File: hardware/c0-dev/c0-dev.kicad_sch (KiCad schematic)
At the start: 0 parts

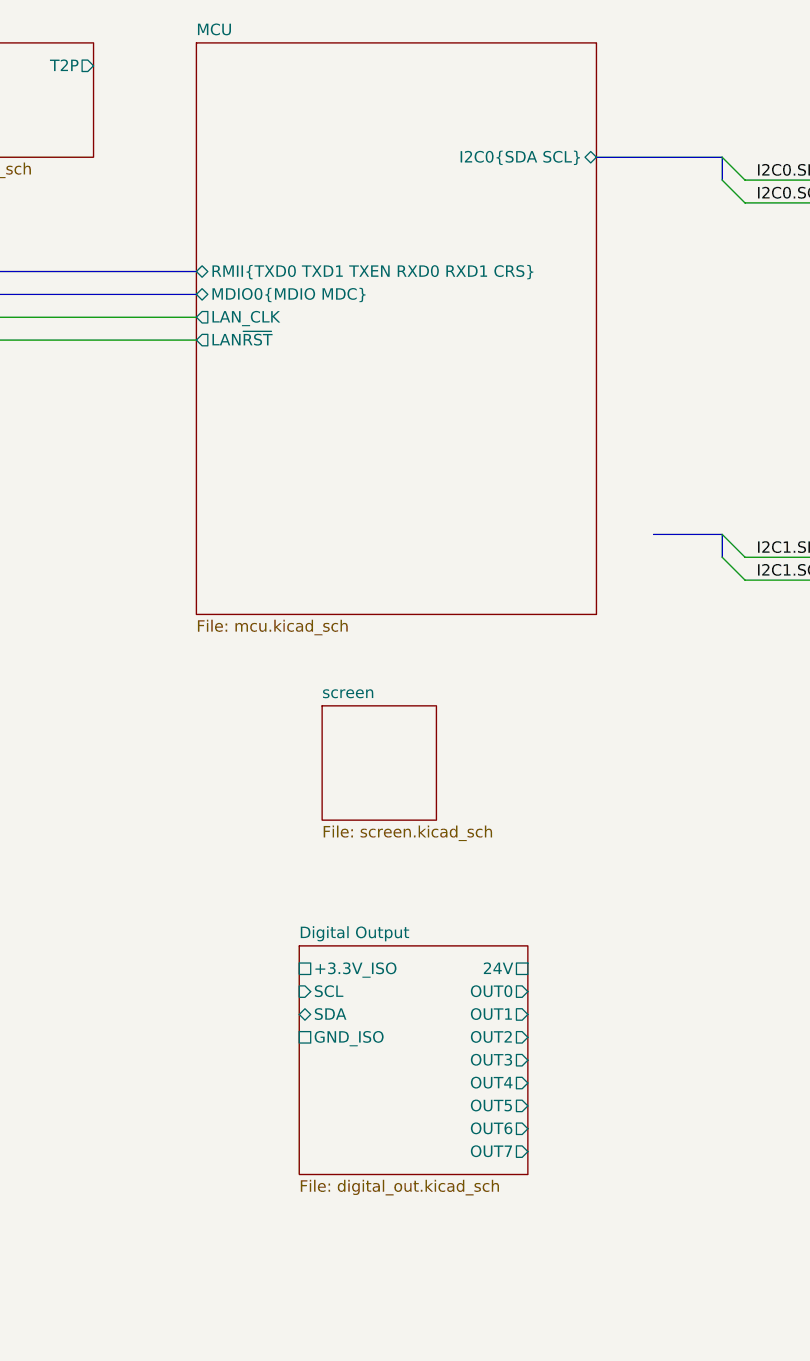
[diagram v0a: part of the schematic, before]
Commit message: introduced MCU isolation netclass
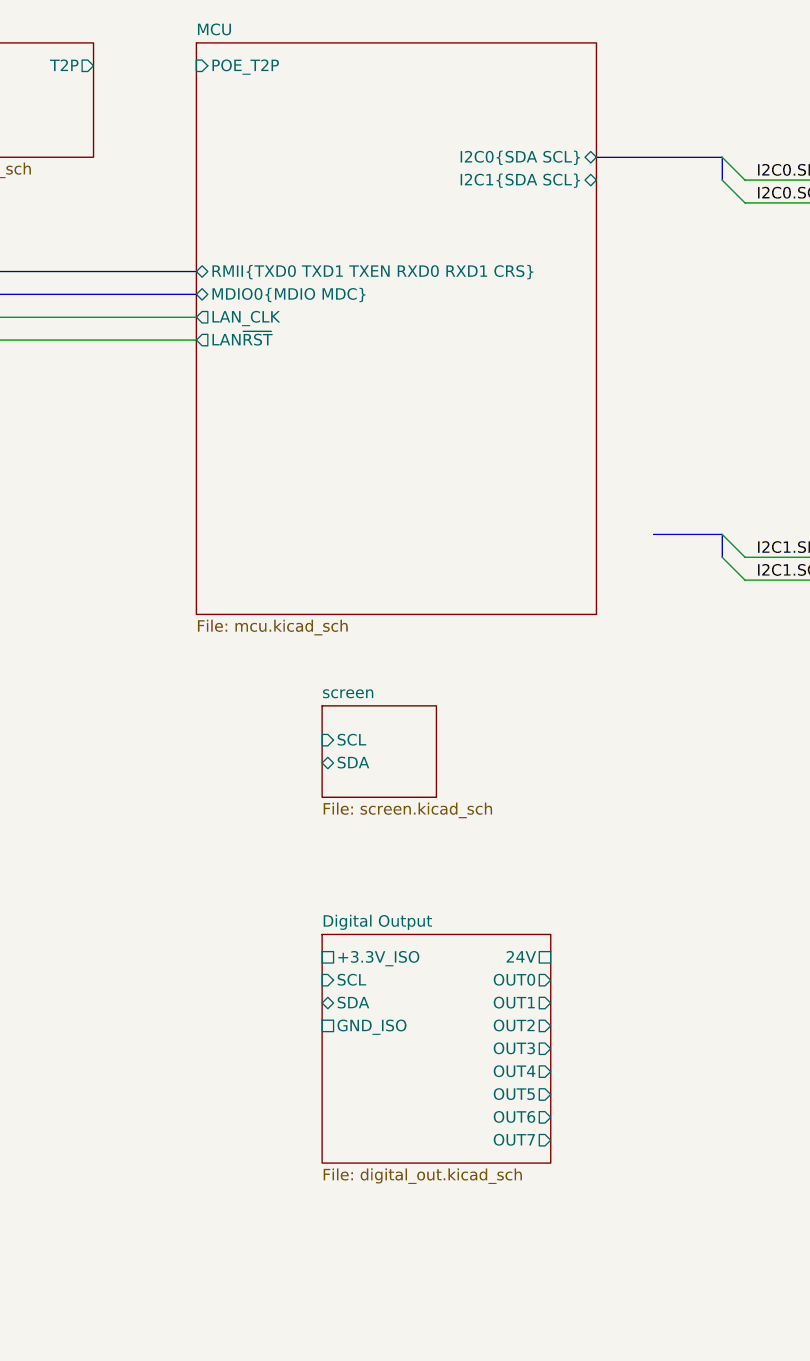
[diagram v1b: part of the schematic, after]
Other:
- sheet MCU ports: added I2C1{SDA SCL}, POE_T2P; removed none
- sheet screen ports: added SCL, SDA; removed none
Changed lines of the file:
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@@
 	)
 	(sheet
-		(at 137.16 128.27)
+		(at 139.7 127)
 		(size 25.4 25.4)
 		(exclude_from_sim no)
@@
 		)
 		(property "Sheetname" "Digital Output"
-			(at 137.16 127.5584 0)
+			(at 139.7 126.2884 0)
 			(show_name no)
 			(do_not_autoplace no)
@@
 		)
 		(property "Sheetfile" "digital_out.kicad_sch"
-			(at 137.16 154.2546 0)
+			(at 139.7 152.9846 0)
 			(show_name no)
 			(do_not_autoplace no)
@@
 		)
 		(pin "SCL" input
-			(at 137.16 133.35 180)
+			(at 139.7 132.08 180)
 			(effects
 				(font
@@
 		)
 		(pin "SDA" bidirectional
-			(at 137.16 135.89 180)
+			(at 139.7 134.62 180)
 			(effects
 				(font
@@
 		)
 		(pin "GND_ISO" passive
-			(at 137.16 138.43 180)
+			(at 139.7 137.16 180)
 			(effects
 				(font
@@
 		)
 		(pin "OUT0" output
-			(at 162.56 133.35 0)
+			(at 165.1 132.08 0)
 			(effects
 				(font
@@
 		)
 		(pin "24V" passive
-			(at 162.56 130.81 0)
+			(at 165.1 129.54 0)
 			(effects
 				(font
@@
 		)
 		(pin "+3.3V_ISO" passive
-			(at 137.16 130.81 180)
+			(at 139.7 129.54 180)
 			(effects
 				(font
@@
 		)
 		(pin "OUT3" output
-			(at 162.56 140.97 0)
+			(at 165.1 139.7 0)
 			(effects
 				(font
@@
 		)
 		(pin "OUT1" output
-			(at 162.56 135.89 0)
+			(at 165.1 134.62 0)
 			(effects
 				(font
@@
 		)
 		(pin "OUT2" output
-			(at 162.56 138.43 0)
+			(at 165.1 137.16 0)
 			(effects
 				(font
@@
 		)
 		(pin "OUT5" output
-			(at 162.56 146.05 0)
+			(at 165.1 144.78 0)
 			(effects
 				(font
@@
 		)
 		(pin "OUT6" output
-			(at 162.56 148.59 0)
+			(at 165.1 147.32 0)
 			(effects
 				(font
@@
 		)
 		(pin "OUT4" output
-			(at 162.56 143.51 0)
+			(at 165.1 142.24 0)
 			(effects
 				(font
@@
 		)
 		(pin "OUT7" output
-			(at 162.56 151.13 0)
+			(at 165.1 149.86 0)
 			(effects
 				(font
@@
 	(sheet
 		(at 139.7 101.6)
-		(size 12.7 12.7)
+		(size 12.7 10.16)
 		(exclude_from_sim no)
 		(in_bom yes)
@@
 		)
 		(property "Sheetfile" "screen.kicad_sch"
-			(at 139.7 114.8846 0)
+			(at 139.7 112.3446 0)
 			(show_name no)
 			(do_not_autoplace no)
@@
 				)
 				(justify left top)
+			)
+		)
+		(pin "SCL" input
+			(at 139.7 105.41 180)
+			(effects
+				(font
+					(size 1.27 1.27)
+				)
+				(justify left)
+			)
+		)
+		(pin "SDA" bidirectional
+			(at 139.7 107.95 180)
+			(effects
+				(font
+					(size 1.27 1.27)
+				)
+				(justify left)
 			)
 		)
@@
 			(effects
 				(font
+					(size 1.27 1.27)
+				)
+				(justify right)
+			)
+		)
+		(pin "POE_T2P" input
+			(at 125.73 30.48 180)
+			(effects
+				(font
+					(size 1.27 1.27)
+				)
+				(justify left)
+			)
+		)
+		(pin "I2C1{SDA SCL}" bidirectional
+			(at 170.18 43.18 0)
+			(effects
+				(font

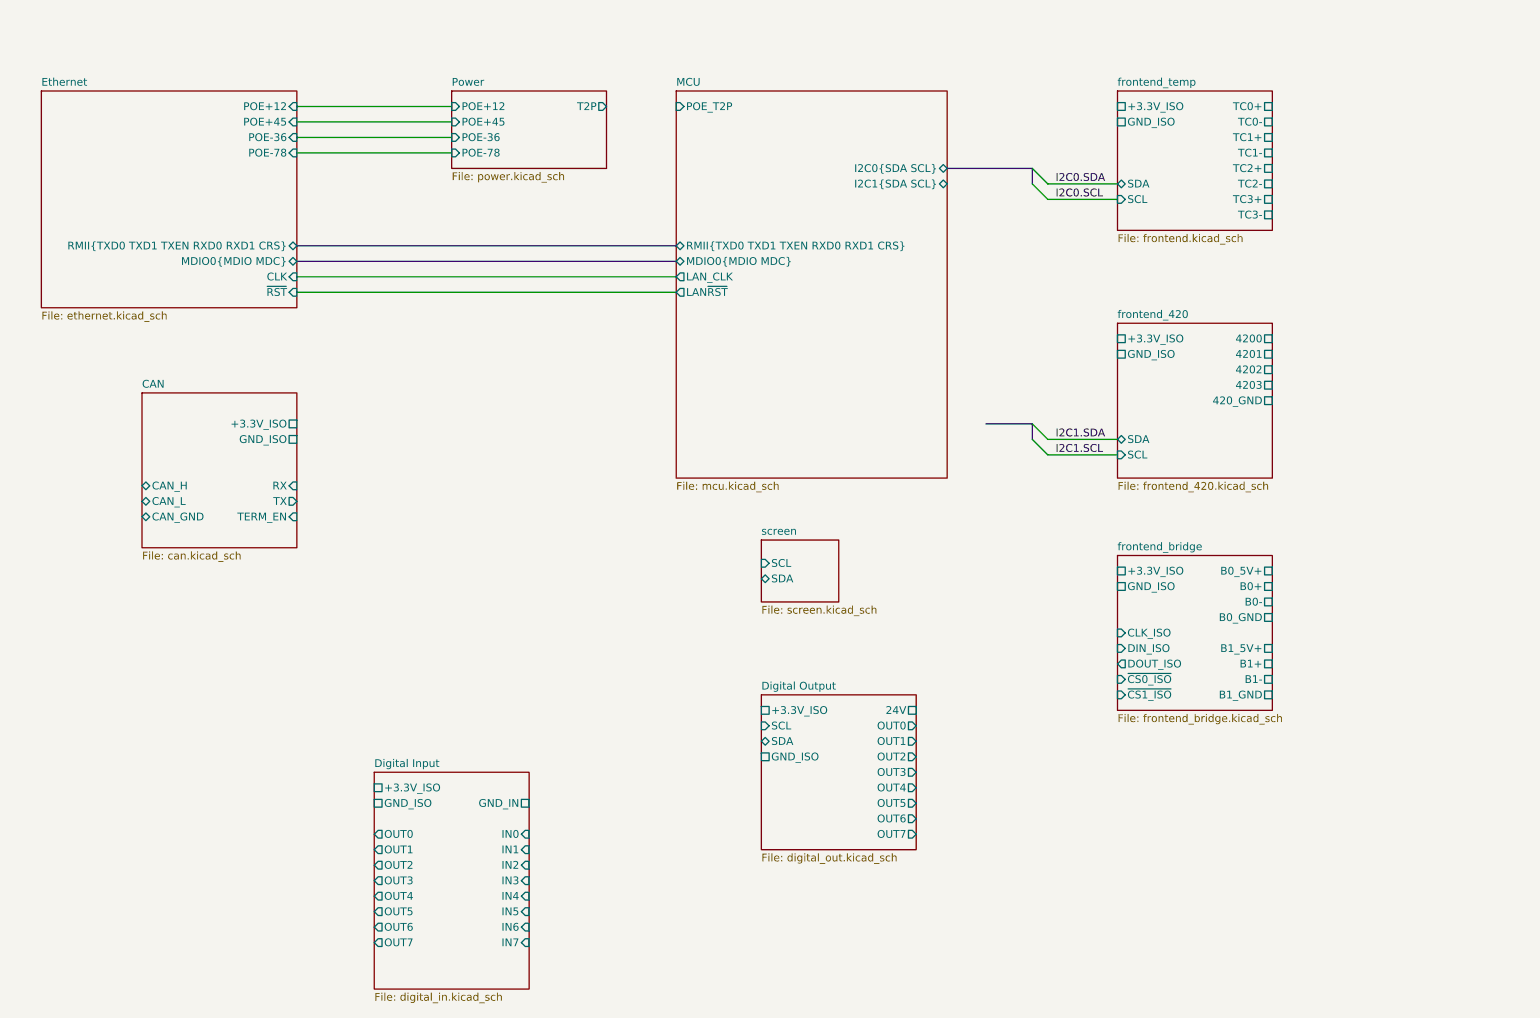
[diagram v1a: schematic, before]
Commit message: connections and i2c clock split
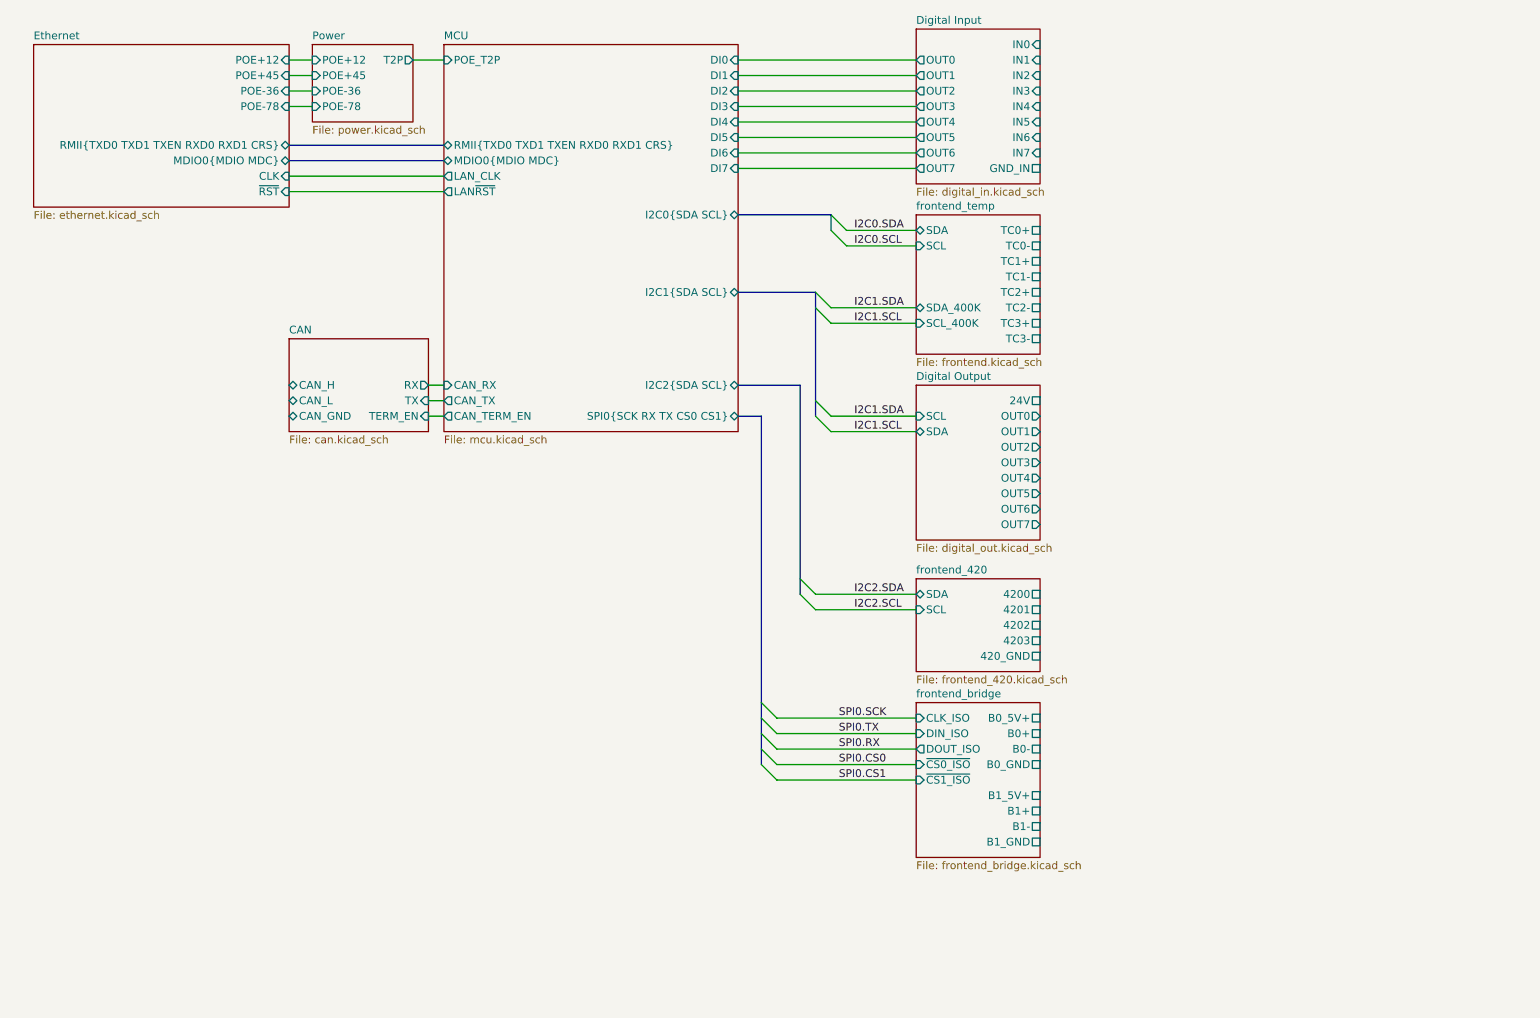
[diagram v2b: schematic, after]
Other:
- removed sheet screen
- sheet CAN ports: added none; removed +3.3V_ISO, GND_ISO
- sheet Digital Input ports: added none; removed +3.3V_ISO, GND_ISO
- sheet Digital Output ports: added none; removed +3.3V_ISO, GND_ISO
- sheet MCU ports: added CAN_RX, CAN_TERM_EN, CAN_TX, DI0, DI1, DI2, DI3, DI4, DI5, DI6, DI7, I2C2{SDA SCL}, SPI0{SCK RX TX CS0 CS1}; removed none
- sheet frontend_420 ports: added none; removed +3.3V_ISO, GND_ISO
- sheet frontend_bridge ports: added none; removed +3.3V_ISO, GND_ISO
- sheet frontend_temp ports: added SCL_400K, SDA_400K; removed +3.3V_ISO, GND_ISO

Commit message: connector
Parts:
- added J3: Conn_01x05, symbol Connector_Generic:Conn_01x05
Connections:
- net CAN/CAN_GND: now also J3.5 (Pin_5)
- net CAN/CAN_H: now also J3.1 (Pin_1), J3.3 (Pin_3)
- net CAN/CAN_L: now also J3.2 (Pin_2), J3.4 (Pin_4)
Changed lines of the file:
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@@
 	(generator_version "10.0")
 	(paper "A4")
+	(text_box "2086-1105/700-000/997-605"
+		(exclude_from_sim no)
+		(at 229.87 63.5 0)
+		(size 35.56 19.05)
+		(margins 0.9525 0.9525 0.9525 0.9525)
+		(stroke
+			(width 0)
+			(type solid)
+		)
+		(fill
+			(type none)
+		)
+		(effects
+			(font
+				(size 1.27 1.27)
+			)
+			(justify left top)
+		)
+	)
+	(junction
+		(at 53.34 78.74)
+		(diameter 0)
+		(color 0 0 0 0)
+	)
+	(junction
+		(at 55.88 76.2)
+		(diameter 0)
+		(color 0 0 0 0)
+	)
 	(bus_entry
 		(at 151.13 50.8)
@@
 	(wire
 		(pts
+			(xy 55.88 76.2) (xy 62.23 76.2)
+		)
+		(stroke
+			(width 0)
+			(type default)
+		)
+	)
+	(wire
+		(pts
 			(xy 151.13 83.82) (xy 165.1 83.82)
 		)
@@
 		)
 	)
+	(wire
+		(pts
+			(xy 49.53 78.74) (xy 53.34 78.74)
+		)
+		(stroke
+			(width 0)
+			(type default)
+		)
+	)
 	(bus
 		(pts
@@
 	(wire
 		(pts
+			(xy 49.53 81.28) (xy 62.23 81.28)
+		)
+		(stroke
+			(width 0)
+			(type default)
+		)
+	)
+	(wire
+		(pts
 			(xy 135.89 38.1) (xy 165.1 38.1)
 		)
@@
 	(wire
 		(pts
+			(xy 53.34 78.74) (xy 62.23 78.74)
+		)
+		(stroke
+			(width 0)
+			(type default)
+		)
+	)
+	(wire
+		(pts
 			(xy 62.23 25.4) (xy 66.04 25.4)
 		)
@@
 		)
 	)
+	(wire
+		(pts
+			(xy 53.34 73.66) (xy 53.34 78.74)
+		)
+		(stroke
+			(width 0)
+			(type default)
+		)
+	)
 	(bus
 		(pts
@@
 	(wire
 		(pts
+			(xy 49.53 71.12) (xy 55.88 71.12)
+		)
+		(stroke
+			(width 0)
+			(type default)
+		)
+	)
+	(wire
+		(pts
 			(xy 62.23 27.94) (xy 66.04 27.94)
 		)
@@
 		)
 	)
+	(wire
+		(pts
+			(xy 55.88 71.12) (xy 55.88 76.2)
+		)
+		(stroke
+			(width 0)
+			(type default)
+		)
+	)
 	(bus
 		(pts
@@
 	(wire
 		(pts
+			(xy 49.53 76.2) (xy 55.88 76.2)
+		)
+		(stroke
+			(width 0)
+			(type default)
+		)
+	)
+	(wire
+		(pts
 			(xy 135.89 30.48) (xy 165.1 30.48)
 		)
@@
 		(pts
 			(xy 62.23 41.91) (xy 87.63 41.91)
+		)
+		(stroke
+			(width 0)
+			(type default)
+		)
+	)
+	(wire
+		(pts
+			(xy 49.53 73.66) (xy 53.34 73.66)
 		)
 		(stroke
@@
 		)
 	)
+	(symbol
+		(lib_id "Connector_Generic:Conn_01x05")
+		(at 44.45 76.2 0)
+		(mirror y)
+		(unit 1)
+		(body_style 1)
+		(exclude_from_sim no)
+		(in_bom yes)
+		(on_board yes)
+		(in_pos_files yes)
+		(dnp no)
+		(fields_autoplaced yes)
+		(property "Reference" "J3"
+			(at 44.45 64.77 0)
+			(show_name no)
+			(do_not_autoplace no)
+			(effects
+				(font
+					(size 1.27 1.27)
+				)
+			)
+		)
+		(property "Value" "Conn_01x05"
+			(at 44.45 67.31 0)
+			(show_name no)
+			(do_not_autoplace no)
+			(effects
+				(font
+					(size 1.27 1.27)
+				)
+			)
+		)
+		(property "Footprint" ""
+			(at 44.45 76.2 0)
+			(hide yes)
+			(show_name no)
+			(do_not_autoplace no)
+			(effects
+				(font
+					(size 1.27 1.27)
+				)
+			)
+		)
+		(property "Datasheet" ""
+			(at 44.45 76.2 0)
+			(hide yes)
+			(show_name no)
+			(do_not_autoplace no)
+			(effects
+				(font
+					(size 1.27 1.27)
+				)
+			)
+		)
+		(property "Description" "Generic connector, single row, 01x05, script generated (kicad-library-utils/schlib/autogen/connector/)"
+			(at 44.45 76.2 0)
+			(hide yes)
+			(show_name no)
+			(do_not_autoplace no)
+			(effects
+				(font
+					(size 1.27 1.27)
+				)
+			)
+		)
+		(pin "5"
+		)
+		(pin "1"
+		)
+		(pin "3"
+		)
+		(pin "4"
+		)
+		(pin "2"
+		)
+		(instances
+			(project "c0-dev"
+				(path "/b8347a0e-ad04-4414-969d-3c64a611d74e"
+					(reference "J3")
+					(unit 1)
+				)
+			)
+		)
+	)
